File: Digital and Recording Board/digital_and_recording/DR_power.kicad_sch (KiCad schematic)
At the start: 3 parts

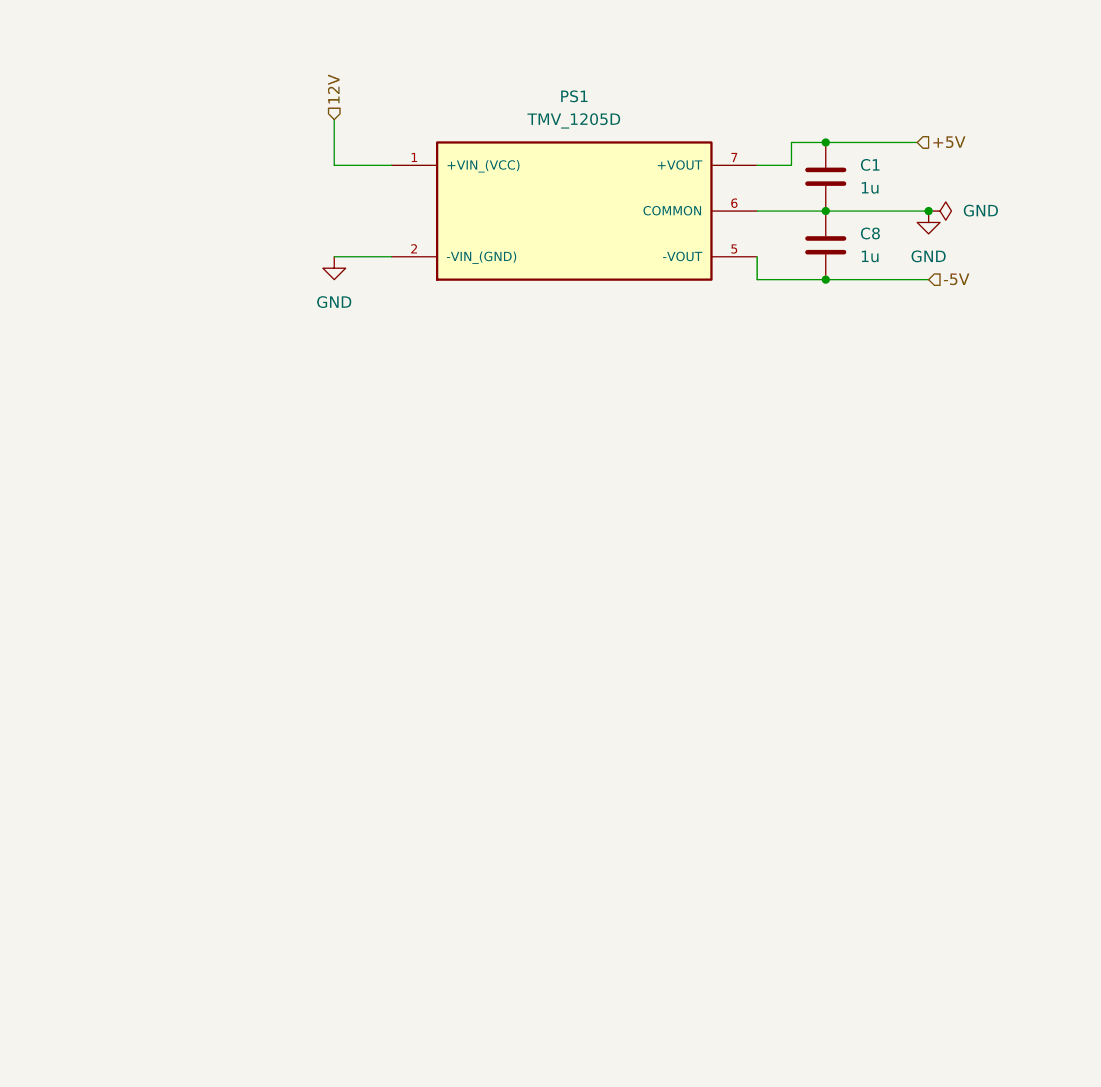
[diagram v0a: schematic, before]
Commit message: modified power for proper amp rating of daisy seed
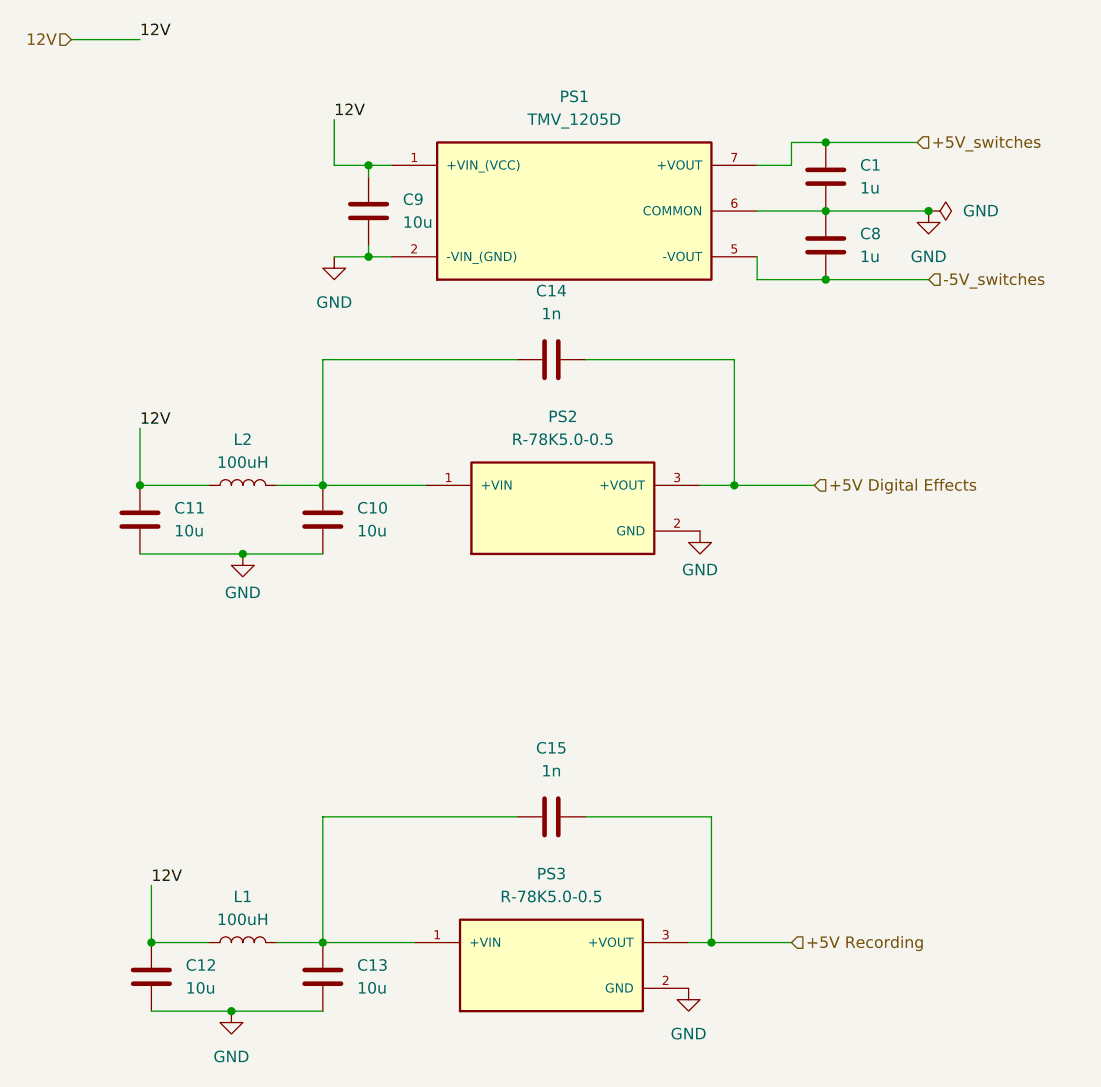
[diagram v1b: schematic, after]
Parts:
- added C10, C11, C12, C13, C9: 10u, Capacitor_SMD:C_0603_1608Metric, symbol Device:C
- added C14, C15: 1n, Capacitor_SMD:C_0603_1608Metric, symbol Device:C
- added L1, L2: 100uH, Inductor_SMD:L_0603_1608Metric, symbol Device:L
- added PS2, PS3: R-78K5.0-0.5, R-78K5.0-0.5:CONV_R-78K5.0-0.5, symbol R-78K5.0-0.5:R-78K5.0-0.5
- C1, C8: footprint Capacitor_SMD:C_0201_0603Metric -> Capacitor_SMD:C_0603_1608Metric
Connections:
- net 12V: now also C11.1, C12.1, C9.1, L1.1, L2.1
- net GND: now also C10.2, C11.2, C12.2, C13.2, C9.2, PS2.2 (GND), PS3.2 (GND)
- net +5V renamed +5V_switches
- net -5V renamed -5V_switches
- new net: C10.1, C14.1, L2.2, PS2.1 (+VIN)
- new net: C13.1, C15.1, L1.2, PS3.1 (+VIN)
- new net +5V Digital Effects: C14.2, PS2.3 (+VOUT)
- new net +5V Recording: C15.2, PS3.3 (+VOUT)
